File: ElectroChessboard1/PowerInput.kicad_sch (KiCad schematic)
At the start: 12 parts, among them J2 TYPE-C-31-M-12, U3 FT232RL

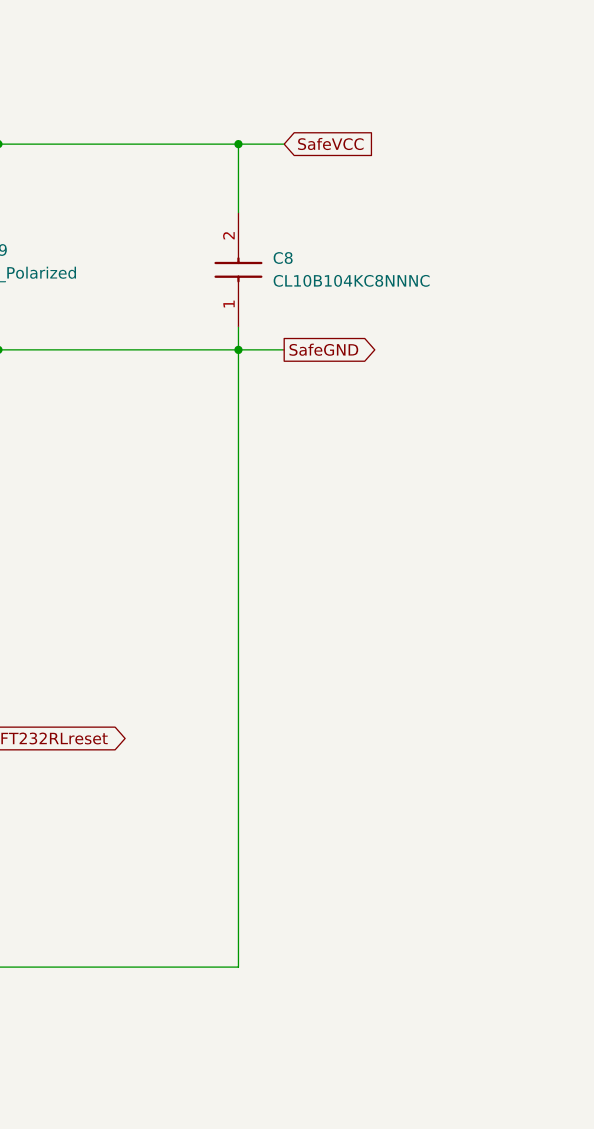
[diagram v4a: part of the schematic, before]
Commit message: Added power status LED
TODO: Move silkscreen texts out of soldiermasks
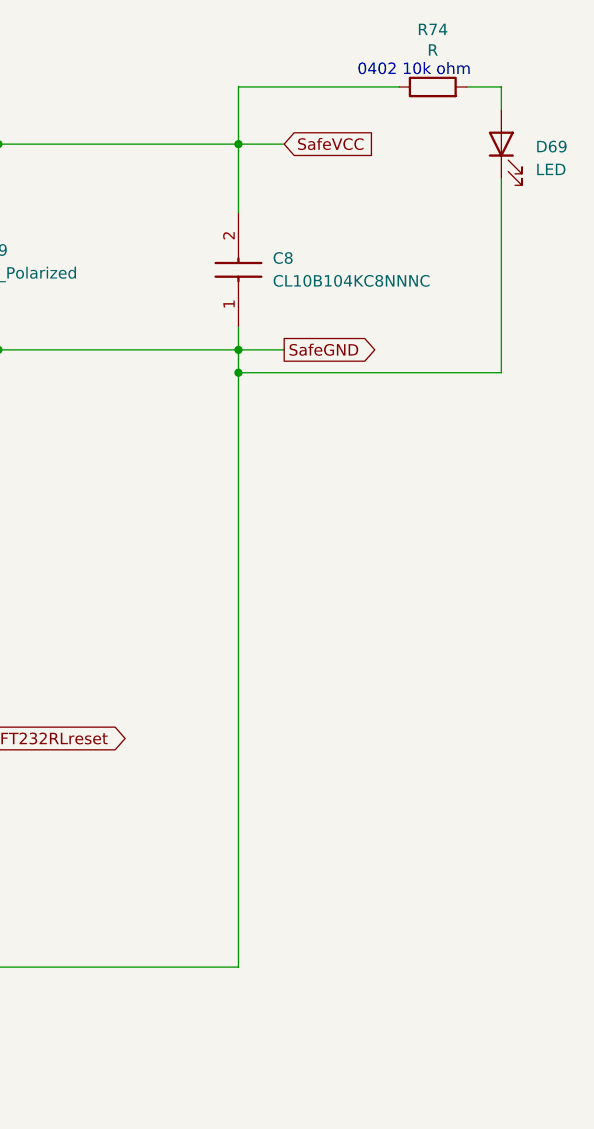
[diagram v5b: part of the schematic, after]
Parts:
- added D69: LED, LED_SMD:LED_0805_2012Metric, symbol Device:LED
- added R74: R, Resistor_SMD:R_0402_1005Metric, symbol Device:R
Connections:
- net GND: now also D69.1 (K)
- net SafeVCC: now also R74.1
- new net: D69.2 (A), R74.2
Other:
- note added: "0402 10k ohm"
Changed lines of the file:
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@@
 		(comment 2 "Elektroniczna szachownica")
+	)
+	(text "0402 10k ohm"
+		(exclude_from_sim no)
+		(at 201.168 28.702 0)
+		(effects
+			(font
+				(size 1.27 1.27)
+			)
+			(justify left)
+		)
 	)
 	(text "Honor Elec RVT1E100M0405\n           RVT1C100M0405"
@@
 	)
 	(junction
+		(at 187.96 62.23)
+		(diameter 0)
+		(color 0 0 0 0)
+	)
+	(junction
 		(at 101.6 128.27)
 		(diameter 0)
@@
 	(wire
 		(pts
-			(xy 187.96 128.27) (xy 187.96 59.69)
+			(xy 187.96 128.27) (xy 187.96 62.23)
 		)
 		(stroke
@@
 	(wire
 		(pts
+			(xy 187.96 30.48) (xy 205.74 30.48)
+		)
+		(stroke
+			(width 0)
+			(type default)
+		)
+	)
+	(wire
+		(pts
 			(xy 127 92.71) (xy 134.62 92.71)
 		)
@@
 	(wire
 		(pts
+			(xy 187.96 62.23) (xy 187.96 59.69)
+		)
+		(stroke
+			(width 0)
+			(type default)
+		)
+	)
+	(wire
+		(pts
 			(xy 109.22 128.27) (xy 111.76 128.27)
 		)
@@
 	(wire
 		(pts
+			(xy 187.96 36.83) (xy 187.96 30.48)
+		)
+		(stroke
+			(width 0)
+			(type default)
+		)
+	)
+	(wire
+		(pts
 			(xy 115.57 44.45) (xy 115.57 36.83)
 		)
@@
 	(wire
 		(pts
+			(xy 217.17 30.48) (xy 217.17 33.02)
+		)
+		(stroke
+			(width 0)
+			(type default)
+		)
+	)
+	(wire
+		(pts
 			(xy 19.05 95.25) (xy 19.05 27.94)
 		)
@@
 	(wire
 		(pts
+			(xy 217.17 40.64) (xy 217.17 62.23)
+		)
+		(stroke
+			(width 0)
+			(type default)
+		)
+	)
+	(wire
+		(pts
 			(xy 52.07 146.05) (xy 67.31 146.05)
 		)
@@
 	(wire
 		(pts
+			(xy 217.17 62.23) (xy 187.96 62.23)
+		)
+		(stroke
+			(width 0)
+			(type default)
+		)
+	)
+	(wire
+		(pts
 			(xy 67.31 139.7) (xy 63.5 139.7)
 		)
@@
 		(pts
 			(xy 134.62 102.87) (xy 140.97 102.87)
+		)
+		(stroke
+			(width 0)
+			(type default)
+		)
+	)
+	(wire
+		(pts
+			(xy 213.36 30.48) (xy 217.17 30.48)
 		)
 		(stroke
@@
 	)
 	(symbol
+		(lib_id "Device:R")
+		(at 209.55 30.48 90)
+		(unit 1)
+		(exclude_from_sim no)
+		(in_bom yes)
+		(on_board yes)
+		(dnp no)
+		(property "Reference" "R74"
+			(at 209.55 24.13 90)
+			(effects
+				(font
+					(size 1.27 1.27)
+				)
+			)
+		)
+		(property "Value" "R"
+			(at 209.55 26.416 90)
+			(effects
+				(font
+					(size 1.27 1.27)
+				)
+			)
+		)
+		(property "Footprint" "Resistor_SMD:R_0402_1005Metric"
+			(at 209.55 32.258 90)
+			(effects
+				(font
+					(size 1.27 1.27)
+				)
+				(hide yes)
+			)
+		)
+		(property "Datasheet" "~"
+			(at 209.55 30.48 0)
+			(effects
+				(font
+					(size 1.27 1.27)
+				)
+				(hide yes)
+			)
+		)
+		(property "Description" "Resistor"
+			(at 209.55 30.48 0)
+			(effects
+				(font
+					(size 1.27 1.27)
+				)
+				(hide yes)
+			)
+		)
+		(pin "1"
+		)
+		(pin "2"
+		)
+		(instances
+			(project "ElectroChessboard1"
+				(path "/b40c7e57-cfb3-41c6-81be-f22d082b0927/90bade89-0322-4f84-b453-80bea2aed5a9"
+					(reference "R74")
+					(unit 1)
+				)
+			)
+		)
+	)
+	(symbol
 		(lib_id "Device:C_Polarized")
 		(at 156.21 50.8 0)
@@
 					(unit 1)
 				)
+			)
+		)
+	)
+	(symbol
+		(lib_id "Device:LED")
+		(at 217.17 36.83 90)
+		(unit 1)
+		(exclude_from_sim no)
+		(in_bom yes)
+		(on_board yes)
+		(dnp no)
+		(fields_autoplaced yes)
+		(property "Reference" "D69"
+			(at 220.98 37.1474 90)
+			(effects
+				(font
+					(size 1.27 1.27)
+				)
+				(justify right)
+			)
+		)
+		(property "Value" "LED"
+			(at 220.98 39.6874 90)
+			(effects
+				(font
+					(size 1.27 1.27)
+				)
+				(justify right)
+			)
+		)
+		(property "Footprint" "LED_SMD:LED_0805_2012Metric"
+			(at 217.17 36.83 0)
+			(effects
+				(font
+					(size 1.27 1.27)
+				)
+				(hide yes)
+			)
+		)
+		(property "Datasheet" "~"
+			(at 217.17 36.83 0)
+			(effects
+				(font
+					(size 1.27 1.27)
+				)
+				(hide yes)
+			)
+		)
+		(property "Description" "Light emitting diode"
+			(at 217.17 36.83 0)
+			(effects
+				(font
+					(size 1.27 1.27)
+				)
+				(hide yes)
+			)
+		)
+		(property "Sim.Pins" "1=K 2=A"
+			(at 217.17 36.83 0)
+			(effects
+				(font
+					(size 1.27 1.27)
+				)
+				(hide yes)
+			)
+		)
+		(pin "2"
+		)
+		(pin "1"
+		)
+		(instances
+			(project "ElectroChessboard1"
+				(path "/b40c7e57-cfb3-41c6-81be-f22d082b0927/90bade89-0322-4f84-b453-80bea2aed5a9"
+					(reference "D69")
+					(unit 1)
+				)

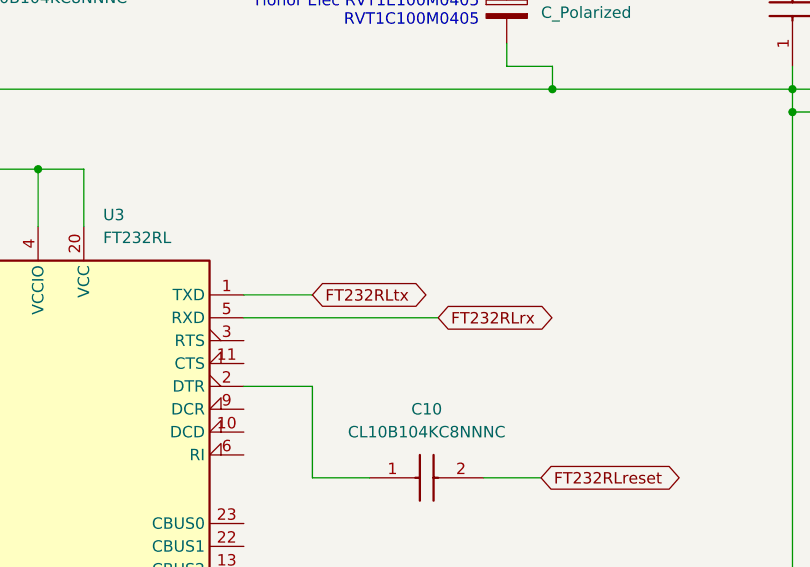
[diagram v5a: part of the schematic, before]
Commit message: Corrected FT-232-RL UART wiring
I wired RX-TX wrong, which made programming via USB not possible and UART available only with SoftwareSerial. Now I corrected that.
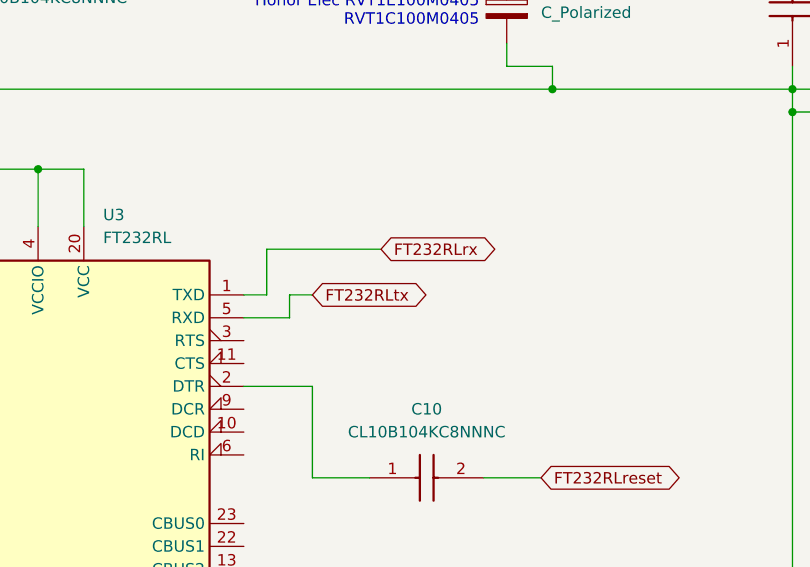
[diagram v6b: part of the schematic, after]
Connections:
- net FT232RLrx: now also U3.1 (TXD); no longer U3.5 (RXD)
- net FT232RLtx: now also U3.5 (RXD); no longer U3.1 (TXD)
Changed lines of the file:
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@@
-	(wire
-		(pts
-			(xy 127 85.09) (xy 148.59 85.09)
-		)
-		(stroke
-			(width 0)
-			(type default)
-		)
-	)
 	(wire
 		(pts
@@
 	(wire
 		(pts
+			(xy 134.62 82.55) (xy 132.08 82.55)
+		)
+		(stroke
+			(width 0)
+			(type default)
+		)
+	)
+	(wire
+		(pts
 			(xy 74.93 109.22) (xy 74.93 127)
 		)
@@
 	(wire
 		(pts
+			(xy 132.08 82.55) (xy 132.08 85.09)
+		)
+		(stroke
+			(width 0)
+			(type default)
+		)
+	)
+	(wire
+		(pts
 			(xy 63.5 132.08) (xy 71.12 132.08)
 		)
@@
 	(wire
 		(pts
+			(xy 129.54 77.47) (xy 129.54 82.55)
+		)
+		(stroke
+			(width 0)
+			(type default)
+		)
+	)
+	(wire
+		(pts
 			(xy 21.59 156.21) (xy 31.75 156.21)
 		)
@@
 	(wire
 		(pts
+			(xy 142.24 77.47) (xy 129.54 77.47)
+		)
+		(stroke
+			(width 0)
+			(type default)
+		)
+	)
+	(wire
+		(pts
 			(xy 67.31 39.37) (xy 92.71 39.37)
 		)
@@
 	(wire
 		(pts
+			(xy 132.08 85.09) (xy 127 85.09)
+		)
+		(stroke
+			(width 0)
+			(type default)
+		)
+	)
+	(wire
+		(pts
 			(xy 106.68 128.27) (xy 109.22 128.27)
 		)
@@
 	(wire
 		(pts
-			(xy 127 82.55) (xy 134.62 82.55)
-		)
-		(stroke
-			(width 0)
-			(type default)
-		)
-	)
-	(wire
-		(pts
 			(xy 67.31 146.05) (xy 67.31 139.7)
+		)
+		(stroke
+			(width 0)
+			(type default)
+		)
+	)
+	(wire
+		(pts
+			(xy 129.54 82.55) (xy 127 82.55)
 		)
 		(stroke
@@
 	(global_label "FT232RLrx"
 		(shape bidirectional)
-		(at 148.59 85.09 0)
+		(at 142.24 77.47 0)
 		(fields_autoplaced yes)
 		(effects
@@
 		)
 		(property "Intersheetrefs" "${INTERSHEET_REFS}"
-			(at 162.4836 85.09 0)
+			(at 156.1336 77.47 0)
 			(effects
 				(font

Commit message: Revert last commit
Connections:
- net FT232RLrx: now also U3.5 (RXD); no longer U3.1 (TXD)
- net FT232RLtx: now also U3.1 (TXD); no longer U3.5 (RXD)
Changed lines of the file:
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@@
+	(wire
+		(pts
+			(xy 127 85.09) (xy 148.59 85.09)
+		)
+		(stroke
+			(width 0)
+			(type default)
+		)
+	)
 	(wire
 		(pts
@@
 	(wire
 		(pts
-			(xy 134.62 82.55) (xy 132.08 82.55)
-		)
-		(stroke
-			(width 0)
-			(type default)
-		)
-	)
-	(wire
-		(pts
 			(xy 74.93 109.22) (xy 74.93 127)
 		)
@@
 	(wire
 		(pts
-			(xy 132.08 82.55) (xy 132.08 85.09)
-		)
-		(stroke
-			(width 0)
-			(type default)
-		)
-	)
-	(wire
-		(pts
 			(xy 63.5 132.08) (xy 71.12 132.08)
 		)
@@
 	(wire
 		(pts
-			(xy 129.54 77.47) (xy 129.54 82.55)
-		)
-		(stroke
-			(width 0)
-			(type default)
-		)
-	)
-	(wire
-		(pts
 			(xy 21.59 156.21) (xy 31.75 156.21)
 		)
@@
 	(wire
 		(pts
-			(xy 142.24 77.47) (xy 129.54 77.47)
-		)
-		(stroke
-			(width 0)
-			(type default)
-		)
-	)
-	(wire
-		(pts
 			(xy 67.31 39.37) (xy 92.71 39.37)
 		)
@@
 	(wire
 		(pts
-			(xy 132.08 85.09) (xy 127 85.09)
-		)
-		(stroke
-			(width 0)
-			(type default)
-		)
-	)
-	(wire
-		(pts
 			(xy 106.68 128.27) (xy 109.22 128.27)
 		)
@@
 	(wire
 		(pts
+			(xy 127 82.55) (xy 134.62 82.55)
+		)
+		(stroke
+			(width 0)
+			(type default)
+		)
+	)
+	(wire
+		(pts
 			(xy 67.31 146.05) (xy 67.31 139.7)
-		)
-		(stroke
-			(width 0)
-			(type default)
-		)
-	)
-	(wire
-		(pts
-			(xy 129.54 82.55) (xy 127 82.55)
 		)
 		(stroke
@@
 	(global_label "FT232RLrx"
 		(shape bidirectional)
-		(at 142.24 77.47 0)
+		(at 148.59 85.09 0)
 		(fields_autoplaced yes)
 		(effects
@@
 		)
 		(property "Intersheetrefs" "${INTERSHEET_REFS}"
-			(at 156.1336 77.47 0)
+			(at 162.4836 85.09 0)
 			(effects
 				(font
